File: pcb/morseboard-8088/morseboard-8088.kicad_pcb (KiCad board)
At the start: 2 copper layers, 172.1 x 108 mm, 90 parts, among them J1 USB_B, J2 CLKSRC, SW1 SW_SPDT, SW2 MANCLK, SW3 RES, SW4 NMI, U1 8088, U10 74HC273, U11 74HC123, U2 74HC573, U3 74HC573, U4 74HC245, U5 SST39SF040, U6 74HC138, U7 74HC02, U8 74HC00, U9 AS6C4008-55PCN, X1 TCXO-14

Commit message: Revising testboard
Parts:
- removed C17: 100uF, Capacitor_THT:CP_Radial_D6.3mm_P2.50mm
- removed C18: 100nF, Capacitor_THT:C_Disc_D5.0mm_W2.5mm_P5.00mm
- removed C19: 1uF, Capacitor_THT:CP_Radial_D5.0mm_P2.50mm
- removed D1, D10, D11, D12, D13, D14, D15, D16, D17, D18, D19, D2, D20, D21, D22, D23, D24, D25, D26, D27, D28, D29, D3, D30, D31, D32, D33, D34, D35, D36, D37, D38, D39, D4, D40, D41, D5, D6, D7, D8: LED, LED_THT:LED_D5.0mm
- removed J2: CLKSRC, Connector_PinHeader_2.54mm:PinHeader_1x03_P2.54mm_Vertical
- removed R3, R5: 10k, Resistor_THT:R_Axial_DIN0207_L6.3mm_D2.5mm_P7.62mm_Horizontal
- removed R4: 47k, Resistor_THT:R_Axial_DIN0207_L6.3mm_D2.5mm_P7.62mm_Horizontal
- removed RN1, RN2, RN3, RN4, RN5: 510, Resistor_THT:R_Array_SIP9
- removed SW2: MANCLK, Button_Switch_THT:SW_PUSH_6mm
- removed U11: 74HC123, Package_DIP:DIP-16_W7.62mm_Socket
- U10: value 74HC273 -> 74HCT273
- U2, U3: value 74HC573 -> 74HCT573
- U4: value 74HC245 -> 74HCT245
- U6: value 74HC138 -> 74HCT138
- U7: value 74HC02 -> 74HCT02
- U8: value 74HC00 -> 74HCT00
- moved C3 12.4 mm to (159.3, 115.8)
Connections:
- X1 pad 8: CLKCAN -> CLK
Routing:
- net D0: track 235.2 -> 36.5 mm, vias 1 -> 0
- net D4: track 220.8 -> 46.6 mm, vias 1 -> 0
- net D3: track 199.7 -> 39.1 mm, vias 2 -> 0
- net A3: track 189.1 -> 28.9 mm, vias 1 -> 0
- net D6: track 201.0 -> 50.8 mm, vias 3 -> 1
- net AD17: track 132.4 -> 7.62 mm, vias 1 -> 0
- net A8: track 146.1 -> 29.4 mm, vias 1 -> 0
- net A5: track 177.1 -> 74.1 mm
- net A13: track 126.9 -> 30.0 mm, vias 3 -> 1
- net AD19: track 104.5 -> 7.62 mm, vias 1 -> 0
- net VCC: track 1113.7 -> 1018.4 mm, vias 0 -> 1
- net CLK: track 121.0 -> 27.7 mm, vias 1 -> 0
- net ~{M}: track 166.1 -> 79.0 mm, vias 3 -> 2
- net DEN: track 137.3 -> 52.7 mm
- net AD16: track 87.3 -> 7.62 mm, vias 2 -> 0
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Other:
- board text added: "REV1"
- board text added: "When populating this board, it is absolutely necessary to use HCT components. HC (not having TTL logics) will **not** work."
- board text removed: "BTN"
- board text removed: "CAN"

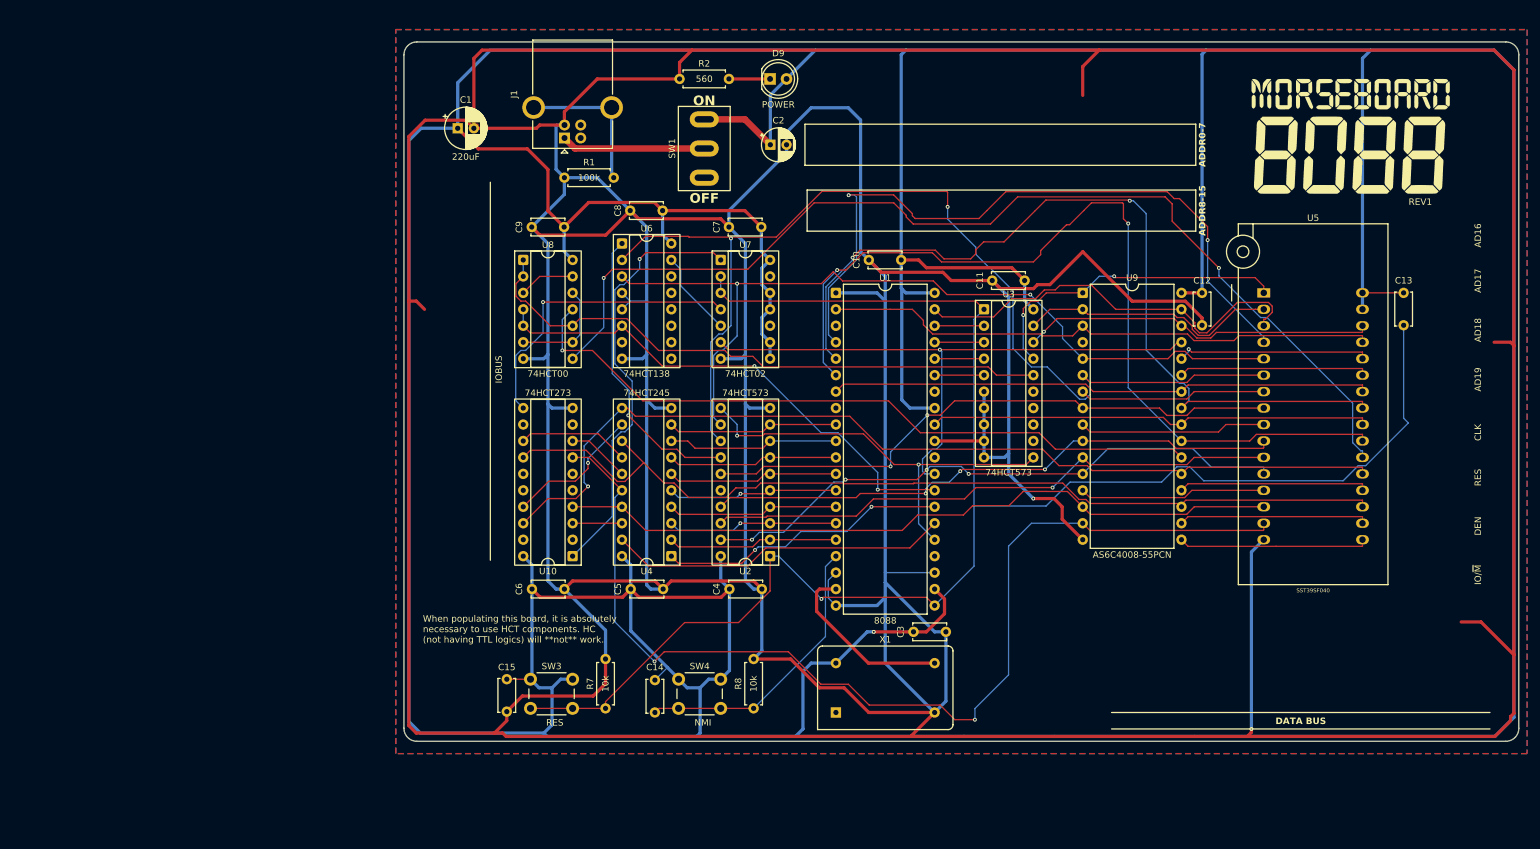
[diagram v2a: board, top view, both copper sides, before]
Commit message: Further revising second 8088 SBC prototype
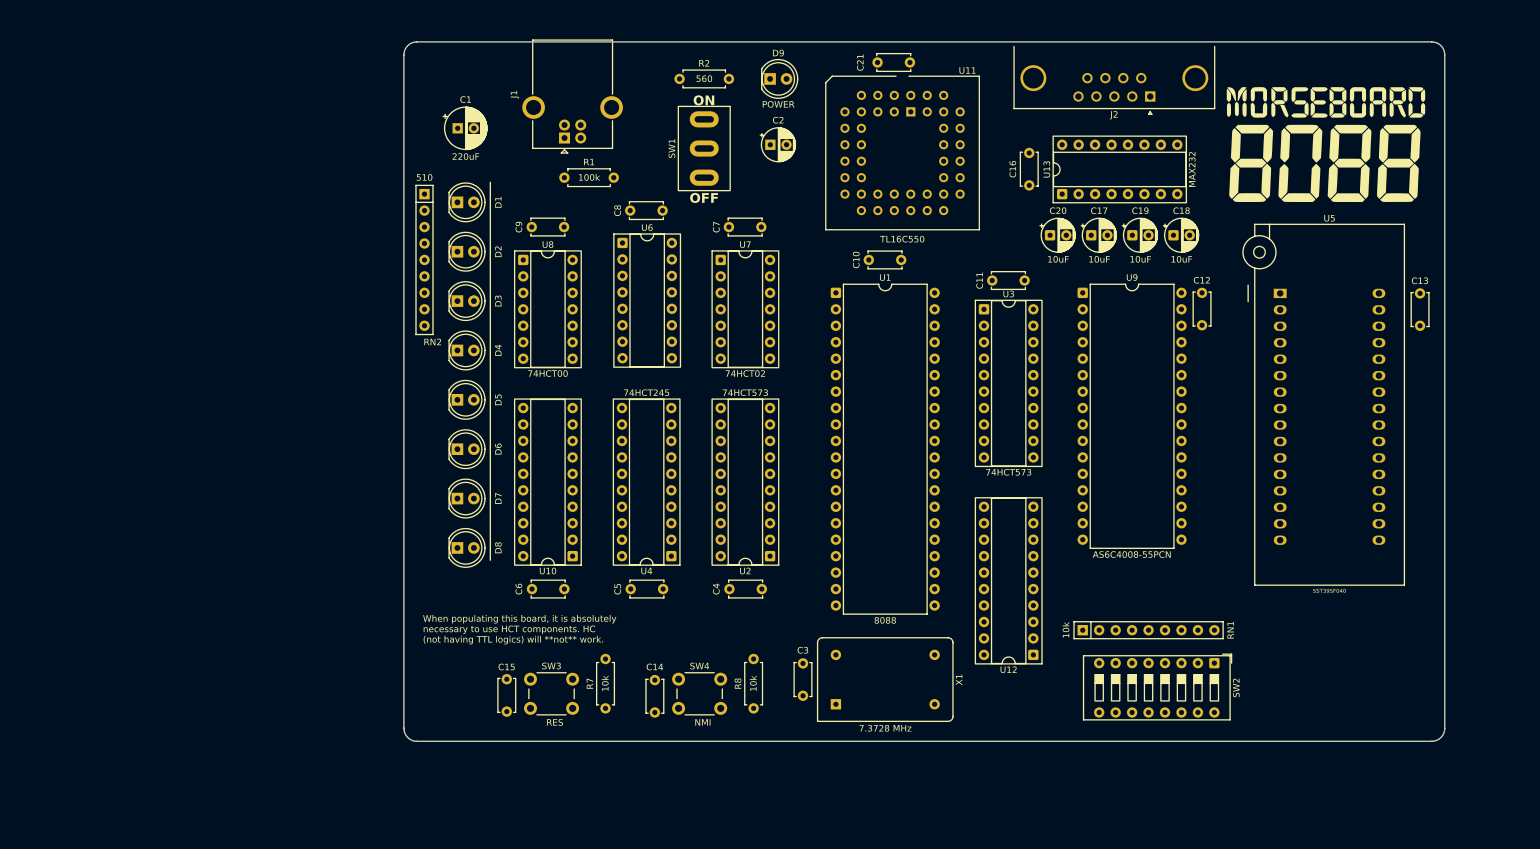
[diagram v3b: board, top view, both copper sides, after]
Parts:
- added C16: 100nF, Capacitor_THT:C_Disc_D5.0mm_W2.5mm_P5.00mm, F.Cu at (177.2, 46.9)
- added C17: 10uF, Capacitor_THT:CP_Radial_D5.0mm_P2.50mm, F.Cu at (186.7, 54.6)
- added C18: 10uF, Capacitor_THT:CP_Radial_D5.0mm_P2.50mm, F.Cu at (199.4, 54.6)
- added C19: 10uF, Capacitor_THT:CP_Radial_D5.0mm_P2.50mm, F.Cu at (193.1, 54.6)
- added C20: 10uF, Capacitor_THT:CP_Radial_D5.0mm_P2.50mm, F.Cu at (180.4, 54.6)
- added C21: 100nF, Capacitor_THT:C_Disc_D5.0mm_W2.5mm_P5.00mm, F.Cu at (158.8, 27.9)
- added D1: LED, LED_THT:LED_D5.0mm, F.Cu at (88.9, 49.5)
- added D2: LED, LED_THT:LED_D5.0mm, F.Cu at (88.9, 57.1)
- added D3: LED, LED_THT:LED_D5.0mm, F.Cu at (88.9, 64.8)
- added D4: LED, LED_THT:LED_D5.0mm, F.Cu at (88.9, 72.4)
- added D5: LED, LED_THT:LED_D5.0mm, F.Cu at (88.9, 80.0)
- added D6: LED, LED_THT:LED_D5.0mm, F.Cu at (88.9, 87.6)
- added D7: LED, LED_THT:LED_D5.0mm, F.Cu at (88.9, 95.2)
- added D8: LED, LED_THT:LED_D5.0mm, F.Cu at (88.9, 102.9)
- added J2: UART1, Connector_Dsub:DSUB-9_Pins_Horizontal_P2.77x2.84mm_EdgePinOffset4.94mm_Housed_MountingHolesOffset4.94mm, F.Cu at (195.8, 33.2)
- added RN1: 10k, Resistor_THT:R_Array_SIP9, F.Cu at (185.4, 115.6)
- added RN2: 510, Resistor_THT:R_Array_SIP9, F.Cu at (83.8, 48.3)
- added SW2: SW_DIP_x08, Button_Switch_THT:SW_DIP_SPSTx08_Slide_9.78x22.5mm_W7.62mm_P2.54mm, F.Cu at (205.7, 120.7)
- added U11: TL16C550, Package_LCC:PLCC-44_THT-Socket, F.Cu at (158.9, 35.6)
- added U12: 74HC245, Package_DIP:DIP-20_W7.62mm_Socket, F.Cu at (177.8, 119.4)
- added U13: MAX232, Package_DIP:DIP-16_W7.62mm_Socket, F.Cu at (182.2, 48.3)
- X1: value TCXO-14 -> 7.3728 MHz
- moved C3 17.7 mm to (142.2, 120.7), turned to -90 degrees
- moved G*** 4.02 mm to (222.9, 40.6)
- moved C13 2.54 mm to (237.5, 68.6)
- moved U5 2.54 mm to (215.9, 63.6)
- moved X1 1.27 mm to (147.3, 127.0)
- moved U6 0.11 mm to (114.4, 55.8)
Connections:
- U1 pad 18: GND -> INTR
- U1 pad 24: unconnected-(U1-~{INTA}-Pad24) -> ~{INTA}
- U6 pad 14: unconnected-(U6-~{Y1}-Pad14) -> ~{IO01}
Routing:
- net GND: track 1354.6 -> 0.00 mm, vias 2 -> 0
- net VCC: track 1018.4 -> 0.00 mm, vias 1 -> 0
- net RES: track 261.9 -> 0.00 mm, vias 1 -> 0
- net D2: track 164.9 -> 0.00 mm, vias 2 -> 0
- net A6: track 164.7 -> 0.00 mm, vias 2 -> 0
- net ~{ROMCS}: track 162.7 -> 0.00 mm, vias 2 -> 0
- net D7: track 147.2 -> 0.00 mm, vias 1 -> 0
- net D5: track 144.2 -> 0.00 mm
- net A10: track 137.7 -> 0.00 mm, vias 2 -> 0
- net A11: track 132.3 -> 0.00 mm, vias 2 -> 0
- net A7: track 131.9 -> 0.00 mm, vias 2 -> 0
- net D1: track 112.6 -> 0.00 mm
- net ~{RAMCS}: track 109.4 -> 0.00 mm, vias 1 -> 0
- net A12: track 108.7 -> 0.00 mm, vias 2 -> 0
- net ~{WR}: track 94.6 -> 0.00 mm, vias 1 -> 0
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- removed copper zone on F.Cu, net GND
- removed copper zone on B.Cu, net VCC
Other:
- board size 172.1 x 108 mm -> 160.7 x 108 mm
- board text removed: "AD16"
- board text removed: "AD17"
- board text removed: "AD18"
- board text removed: "AD19"
- board text removed: "ADDR0-7"
- board text removed: "ADDR8-15"
- board text removed: "CLK"
- board text removed: "DATA BUS"
- board text removed: "DEN"
- board text removed: "IO/~{M}"
- board text removed: "IOBUS"
- board text removed: "RES"
- board text removed: "REV1"

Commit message: Updating schematic and board
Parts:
- removed G***: LOGO, components:morseboard-logo
- added H1: MountingHole, MountingHole:MountingHole_3.2mm_M3_DIN965, F.Cu at (83.8, 27.9)
- added H2: MountingHole, MountingHole:MountingHole_3.2mm_M3_DIN965, F.Cu at (238.5, 27.9)
- added H3: MountingHole, MountingHole:MountingHole_3.2mm_M3_DIN965, F.Cu at (83.8, 129.5)
- added H4: MountingHole, MountingHole:MountingHole_3.2mm_M3_DIN965, F.Cu at (238.5, 129.5)
- added J3: TxD, Connector_PinHeader_2.54mm:PinHeader_1x03_P2.54mm_Vertical, F.Cu at (211.3, 42.2)
- added J4: ~{CTS}, Connector_PinHeader_2.54mm:PinHeader_1x03_P2.54mm_Vertical, F.Cu at (219.4, 42.1)
- added J5: RxD, Connector_PinHeader_2.54mm:PinHeader_1x03_P2.54mm_Vertical, F.Cu at (227.6, 42.1)
- added J6: ~{RTS}, Connector_PinHeader_2.54mm:PinHeader_1x03_P2.54mm_Vertical, F.Cu at (235.7, 42.2)
- SW2: value SW_DIP_x08 -> INTPORT
- U1: footprint Package_DIP:DIP-40_W15.24mm -> Package_DIP:DIP-40_W15.24mm_Socket
- U9: footprint Package_DIP:DIP-32_W15.24mm -> Package_DIP:DIP-32_W15.24mm_Socket
- moved C13 16.1 mm to (222.5, 62.5), turned to 0 degrees
- moved U5 13.4 mm to (217.6, 76.8)
- moved C12 6.42 mm to (206.5, 69.3)
- moved U9 6.42 mm to (188.1, 69.3)
- moved C21 1.52 mm to (160.3, 27.9)
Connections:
- J2 pad 2: Net-(U13-T1OUT) -> UART2
- J2 pad 3: Net-(U13-R1IN) -> UART3
- J2 pad 7: unconnected-(J2-Pad7) -> UART7
- J2 pad 8: unconnected-(J2-Pad8) -> UART8
- U11 pad 36: unconnected-(U11-~{RTS}-Pad36) -> ~{RTS}
- U11 pad 40: unconnected-(U11-~{CTS}-Pad40) -> ~{CTS}
- U13 pad 10: unconnected-(U13-T2IN-Pad10) -> ~{CTS}
- U13 pad 13: Net-(U13-R1IN) -> R1IN
- U13 pad 14: Net-(U13-T1OUT) -> T1OUT
- U13 pad 7: unconnected-(U13-T2OUT-Pad7) -> T2OUT
- U13 pad 8: unconnected-(U13-R2IN-Pad8) -> R2IN
- U13 pad 9: unconnected-(U13-R2OUT-Pad9) -> ~{RTS}
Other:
- board size 160.7 x 108 mm -> 161 x 108 mm
- board text added: "UART2"
- board text added: "UART3"
- board text added: "UART7"
- board text added: "UART8"

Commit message: Prerouting commit
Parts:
- removed C13: 100nF, Capacitor_THT:C_Disc_D5.0mm_W2.5mm_P5.00mm
- removed R7: 10k, Resistor_THT:R_Axial_DIN0207_L6.3mm_D2.5mm_P7.62mm_Horizontal
- removed SW3: RES, Button_Switch_THT:SW_PUSH_6mm
- added G***: LOGO, components:morseboard-logo-12h, F.Cu at (223.5, 32.0)
- added SW6: RESET, Button_Switch_THT:SW_PUSH_6mm, F.Cu at (102.7, 123.2)
- added U14: DS1813, Package_TO_SOT_THT:TO-92, F.Cu at (95.8, 125.8)
- moved C15 144.2 mm to (227.5, 63.0), turned to 180 degrees
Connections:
- U13 pad 10: ~{CTS} -> ~{RTS}
- U13 pad 9: ~{RTS} -> ~{CTS}
- U7 pad 1: ~{RES} -> RES
- U7 pad 2: RES -> ~{RES}
- U7 pad 3: RES -> ~{RES}
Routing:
- net GND: track 0.00 -> 1207.3 mm, vias 0 -> 2
- net VCC: track 0.00 -> 1064.8 mm
- net CLK: track 0.00 -> 82.9 mm
- net VIN: track 0.00 -> 24.1 mm
- net Net-(J1-Shield): track 0.00 -> 23.0 mm
- net Net-(U13-VS-): track 0.00 -> 9.62 mm
- net Net-(U13-C1-): track 0.00 -> 8.19 mm
- net Net-(U13-C2+): track 0.00 -> 7.68 mm
- net Net-(U13-C2-): track 0.00 -> 7.67 mm
- net Net-(U13-VS+): track 0.00 -> 7.16 mm
- net Net-(U13-C1+): track 0.00 -> 7.12 mm
- net Net-(D9-K): track 0.00 -> 6.35 mm
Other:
- board text added: "RxD"
- board text added: "Set regular or null-modem serial configuration. Squares indicate regular configuration."
- board text added: "TxD"
- board text added: "~{CTS}"
- board text added: "~{RTS}"

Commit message: Protoype #1 of SBC
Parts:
- added C13: 100nF, Capacitor_THT:C_Disc_D5.0mm_W2.5mm_P5.00mm, F.Cu at (171.5, 124.5)
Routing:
- net D7: track 0.00 -> 276.9 mm, vias 0 -> 1
- net D5: track 0.00 -> 271.1 mm, vias 0 -> 2
- net D6: track 0.00 -> 263.0 mm, vias 0 -> 2
- net D4: track 0.00 -> 255.8 mm, vias 0 -> 1
- net D2: track 0.00 -> 248.0 mm, vias 0 -> 2
- net D3: track 0.00 -> 229.2 mm, vias 0 -> 2
- net D1: track 0.00 -> 208.1 mm, vias 0 -> 1
- net GND: track 1207.3 -> 1415.0 mm
- net D0: track 0.00 -> 198.0 mm, vias 0 -> 1
- net ~{ROMCS}: track 0.00 -> 172.6 mm, vias 0 -> 1
- net A1: track 0.00 -> 170.1 mm, vias 0 -> 3
- net A6: track 0.00 -> 154.3 mm
- net RES: track 0.00 -> 148.0 mm, vias 0 -> 2
- net A5: track 0.00 -> 147.0 mm
- net A0: track 0.00 -> 145.1 mm, vias 0 -> 1
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- added copper zone on F.Cu, net GND
- added copper zone on B.Cu, net VCC
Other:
- board text added: "Configure interrupt vector for UART"
- board text added: "jlcjlcjlcjlc"

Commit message: Interim commit
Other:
- board text added: "Set jumper to rectangular boxes for regular serial cable."
- board text removed: "Set regular or null-modem serial configuration. Squares indicate regular configuration."
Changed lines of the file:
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@@
 	(gr_rect
 		(start 213.106 41.148)
-		(end 214.376 42.672)
+		(end 214.376 45.847)
 		(stroke
 			(width 0.1)
@@
 	)
 	(gr_rect
-		(start 229.362 46.609)
-		(end 230.632 48.133)
+		(start 220.98 44.0055)
+		(end 222.25 48.7045)
 		(stroke
 			(width 0.1)
@@
 	)
 	(gr_rect
-		(start 237.49 46.609)
-		(end 238.76 48.133)
+		(start 229.235 44.0055)
+		(end 230.505 48.7045)
 		(stroke
 			(width 0.1)
@@
 	)
 	(gr_rect
-		(start 221.234 41.148)
-		(end 222.504 42.672)
+		(start 237.49 41.0695)
+		(end 238.76 45.7685)
 		(stroke
 			(width 0.1)
@@
 		)
 	)
-	(gr_text "Set regular or null-modem \nserial configuration. Squares \nindicate regular configuration."
-		(at 212.217 56.007 0)
+	(gr_text "Set jumper to rectangular boxes \nfor regular serial cable."
+		(at 210.82 53.975 0)
 		(layer "F.SilkS")
 		(effects

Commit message: Fixing bugs in PCB design
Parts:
- removed J3: TxD, Connector_PinHeader_2.54mm:PinHeader_1x03_P2.54mm_Vertical
- removed J4: ~{CTS}, Connector_PinHeader_2.54mm:PinHeader_1x03_P2.54mm_Vertical
- removed J5: RxD, Connector_PinHeader_2.54mm:PinHeader_1x03_P2.54mm_Vertical
- removed J6: ~{RTS}, Connector_PinHeader_2.54mm:PinHeader_1x03_P2.54mm_Vertical
- moved G*** 138.3 mm to (88.9, 63.5)
- moved U5 109.9 mm to (116.8, 33.0)
- moved D9 106.7 mm to (30.5, 34.3)
- moved C19 101.8 mm to (91.4, 49.5)
- moved C18 101.8 mm to (97.8, 49.5)
- moved C20 101.8 mm to (78.7, 49.5)
- moved U13 101.8 mm to (80.6, 43.2)
- moved C16 101.8 mm to (75.5, 41.8)
- moved C17 101.8 mm to (85.1, 49.5)
- moved J2 101.5 mm to (94.4, 28.8)
- moved U11 100.4 mm to (59.7, 50.8)
- moved SW1 96.5 mm to (31.8, 56.5)
- moved C2 96.3 mm to (42.0, 26.7)
- moved H4 96.0 mm to (143.5, 143.5)
- moved H2 95.1 mm to (143.5, 24.1)
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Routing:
- net D7: track 276.9 -> 0.00 mm, vias 1 -> 0
- net D5: track 271.1 -> 0.00 mm, vias 2 -> 0
- net D6: track 263.0 -> 0.00 mm, vias 2 -> 0
- net D4: track 255.8 -> 0.00 mm, vias 1 -> 0
- net D2: track 248.0 -> 0.00 mm, vias 2 -> 0
- net D3: track 229.2 -> 0.00 mm, vias 2 -> 0
- net D1: track 208.1 -> 0.00 mm, vias 1 -> 0
- net D0: track 198.0 -> 0.00 mm, vias 1 -> 0
- net ~{ROMCS}: track 172.6 -> 0.00 mm, vias 1 -> 0
- net A1: track 170.1 -> 0.00 mm, vias 3 -> 0
- net A6: track 154.3 -> 0.00 mm
- net RES: track 148.0 -> 0.00 mm, vias 2 -> 0
- net A5: track 147.0 -> 0.00 mm
- net A0: track 145.1 -> 0.00 mm, vias 1 -> 0
- net A2: track 138.8 -> 0.00 mm, vias 1 -> 0
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- removed copper zone on F.Cu, net GND
- removed copper zone on B.Cu, net VCC
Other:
- board size 161 x 108 mm -> 127 x 127 mm
- board text added: "rev1"
- board text removed: "RxD"
- board text removed: "Set jumper to rectangular boxes for regular serial cable."
- board text removed: "TxD"
- board text removed: "UART2"
- board text removed: "UART3"
- board text removed: "UART7"
- board text removed: "UART8"
- board text removed: "~{CTS}"
- board text removed: "~{RTS}"
